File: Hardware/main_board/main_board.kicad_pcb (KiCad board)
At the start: 6 copper layers, 95.4 x 36.1 mm, 282 parts, among them J1 BATT, J2 LCD, J3 BACK_LIGHT, J4 SD, J5 NFC, J6 EXT1, J7 EXT0, J8 USB_C, Q1 DMN313DLT, SW1 OK, SW2 BACK, SW3 RIGHT, SW4 LEFT, SW5 UP, SW6 DOWN, T1 B0310J50100AHF, U1 STM32WB55RGVx, U10 BGS13S4N9E6327XTSA1, U11 NC7SZ32M5X, U12 LP5562TMX, U2 BQ27220YZFR, U3 BQ25896RTWR, U4 RS3221-3.3YF3, U5 LM66100DCK, U6 LM3281YFQR, U7 LM3281YFQR, U8 CC1101RGP, U9 BGS13S4N9E6327XTSA1, Y1 32MHz, Y2 32.768K, Y3 26MHz

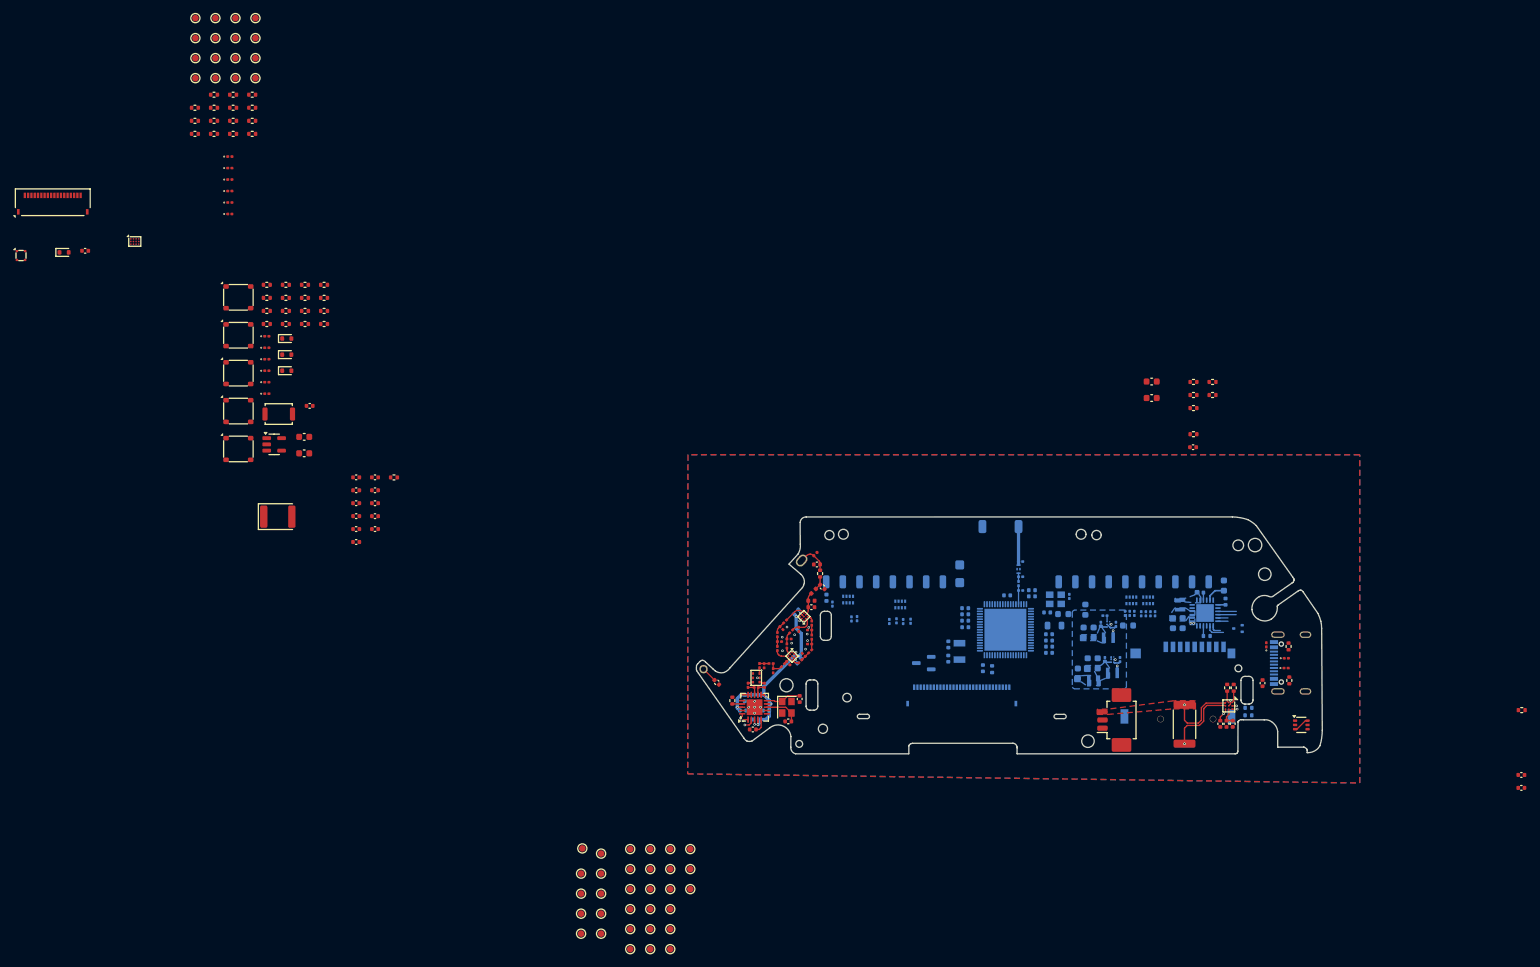
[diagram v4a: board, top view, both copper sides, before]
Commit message: layout: layout bms and buttons
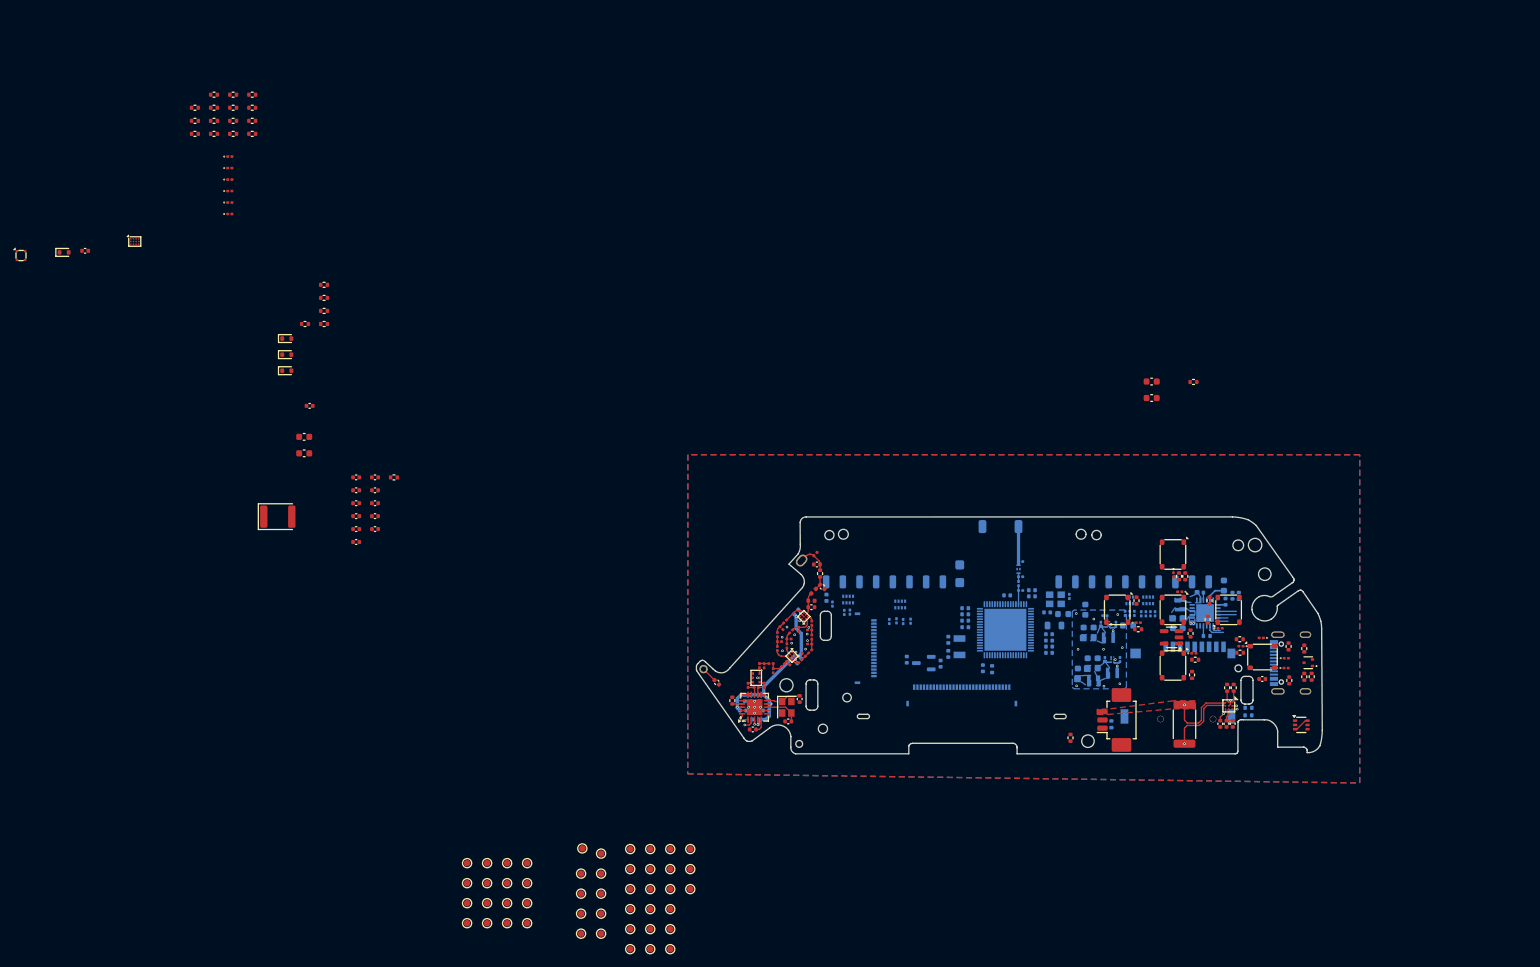
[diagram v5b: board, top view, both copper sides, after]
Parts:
- C28, C32, C33, J5, R10, R9: moved to B.Cu
- Q1: moved to F.Cu
- SW1: footprint Button_Switch_SMD:SW_Push_SPST_NO_Alps_SKRK -> Library:SW_Push_SPST_NO_Alps_ SKRM
- moved SW2 165.4 mm to (254.0, 134.3)
- moved R19 157.8 mm to (250.5, 131.6), turned to 180 degrees
- moved SW3 156.6 mm to (248.8, 127.1), turned to 90 degrees
- moved D2 155.2 mm to (250.7, 132.6), turned to 180 degrees
- moved R25 154.4 mm to (250.6, 133.6)
- moved R20 151.5 mm to (245.6, 128.6), turned to 90 degrees
- moved D3 150.9 mm to (247.5, 129.9)
- moved R23 149.9 mm to (243.7, 134.7)
- moved R24 147.0 mm to (243.0, 130.7), turned to 90 degrees
- moved R26 146.9 mm to (245.9, 125.7), turned to -90 degrees
- moved D6 146.7 mm to (243.5, 133.7)
- moved SW6 146.2 mm to (240.3, 135.6), turned to -90 degrees
- moved R29 146.1 mm to (243.3, 137.0), turned to -90 degrees
- moved R22 145.1 mm to (242.2, 122.0), turned to -90 degrees
- moved D1 144.5 mm to (241.4, 124.3), turned to 180 degrees
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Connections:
- Q1 pad 1: Net-(Q1-D) -> Net-(Q1-G)
- Q1 pad 2: Net-(Q1-G) -> GND
- Q1 pad 3: GND -> Net-(Q1-D)
- R12 pad 1: SYS -> VSYS
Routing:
- net GNDP: vias 0 -> 9

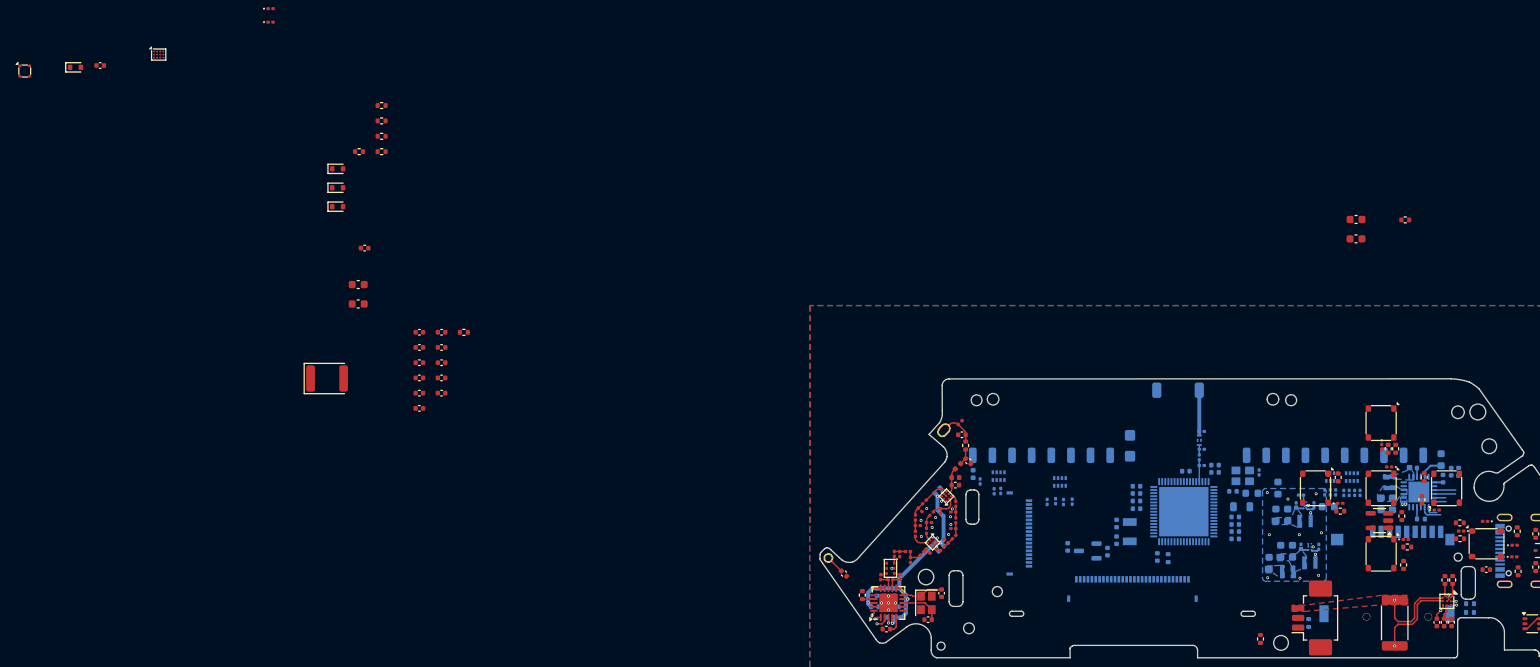
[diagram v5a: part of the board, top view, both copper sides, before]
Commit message: layout: place the led driver
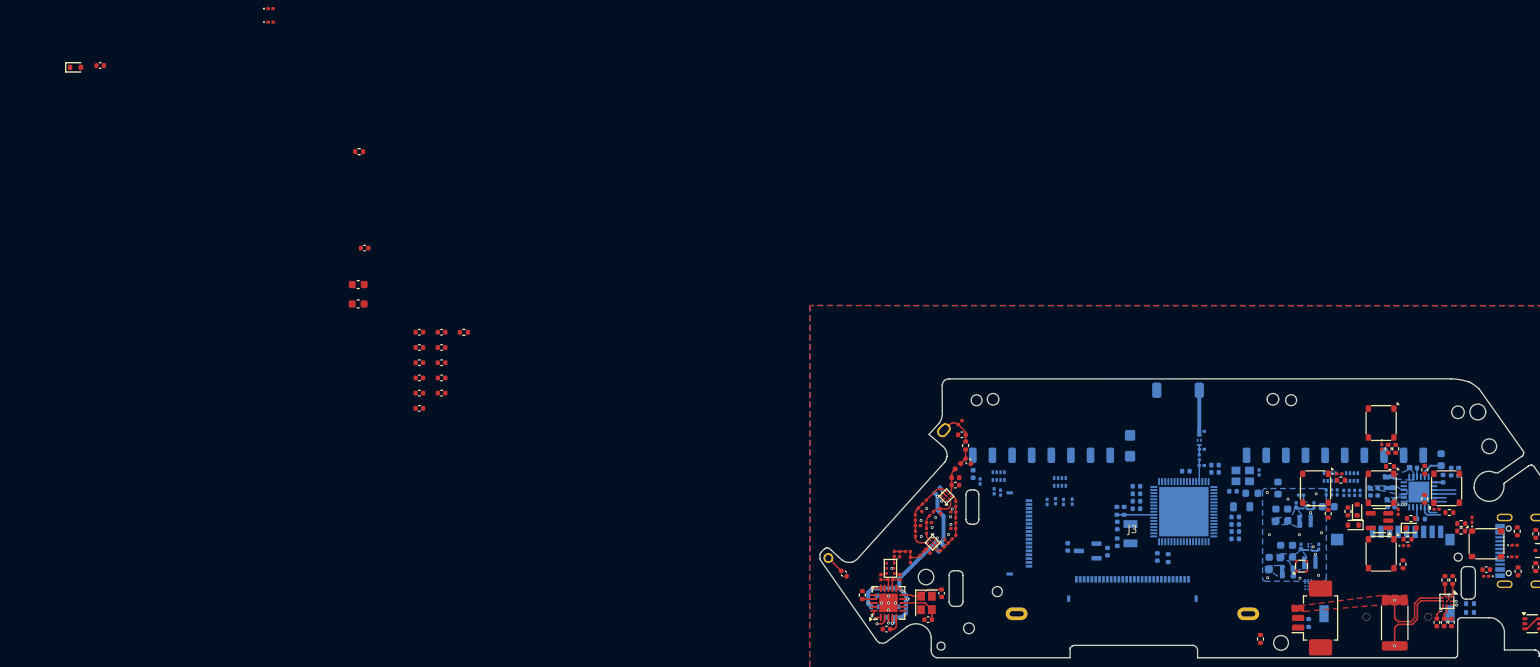
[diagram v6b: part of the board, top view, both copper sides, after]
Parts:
- C20, C21: footprint Capacitor_SMD:C_0603_1608Metric -> Capacitor_SMD:C_0402_1005Metric
- C26, C27: footprint Capacitor_SMD:C_0603_1608Metric -> Capacitor_SMD:C_0402_1005Metric; moved to B.Cu
- J3: footprint LED_SMD:LED_1812_4532Metric -> Library:ERC12864FAMF03
- R31, R33, U12: moved to B.Cu
- moved D10 177.2 mm to (230.1, 137.2), turned to 90 degrees
- moved U12 163.8 mm to (230.9, 139.6), turned to 90 degrees
- moved D7 146.5 mm to (244.2, 132.2)
- moved R32 142.8 mm to (244.2, 131.0)
- moved D8 138.5 mm to (236.8, 131.9), turned to 180 degrees
- moved D9 137.6 mm to (237.2, 129.9), turned to 90 degrees
- moved R34 133.4 mm to (236.1, 130.1), turned to 90 degrees
- moved R31 108.6 mm to (206.2, 130.0), turned to 90 degrees
- moved J3 108.6 mm to (208.2, 143.3)
- moved R33 107.6 mm to (207.1, 130.0), turned to 90 degrees
- moved R8 38.3 mm to (249.2, 130.2)
- moved C26 37.1 mm to (242.1, 129.1), turned to 90 degrees
- moved C27 34.5 mm to (241.2, 129.1), turned to 90 degrees
- moved D33 7.11 mm to (253.9, 138.5)
- moved R24 6.60 mm to (241.5, 124.3), turned to 0 degrees
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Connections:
- J3 pad 1: Net-(J3-Pin_1) -> /LCD/LCD_LED
- J3 pad 2: /LCD/LCD_LED -> Net-(J3-A)
- R26 pad 1: /Buttons/BUTTON_LEFT -> /Buttons/BUTTON_RIGHT
- R27 pad 1: /Buttons/BUTTON_RIGHT -> /Buttons/BUTTON_LEFT
- R35 pad 1: Net-(J3-Pin_1) -> Net-(J3-A)
- RN2 pad 5: unconnected-(RN2-Pad5) -> /MCU/UART1_TX
- RN2 pad 6: /MCU/SWCLK -> /MCU/SWDIO
- RN2 pad 7: /MCU/SWDIO -> /MCU/SWCLK
- RN2 pad 8: /MCU/UART1_TX -> unconnected-(RN2-Pad8)
- RN3 pad 5: /MCU/PA4 -> /MCU/PC3
- RN3 pad 6: /MCU/PB3 -> /MCU/PB2
- RN3 pad 7: /MCU/PB2 -> /MCU/PB3
- RN3 pad 8: /MCU/PC3 -> /MCU/PA4
- RN4 pad 5: /MCU/UART1_RX -> /MCU/iBTN
- RN4 pad 6: /MCU/PC1 -> /MCU/PC0
- RN4 pad 7: /MCU/PC0 -> /MCU/PC1
- RN4 pad 8: /MCU/iBTN -> /MCU/UART1_RX
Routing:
- net /Buttons/RESET: track 0.00 -> 4.78 mm
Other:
- outline, holes or cut-outs redrawn
